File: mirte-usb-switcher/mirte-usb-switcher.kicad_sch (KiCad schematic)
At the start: 5 parts, among them J1 Conn_02x02_Counter_Clockwise, U1 SIP32509DT-T1-GE3

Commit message: move usb switcher
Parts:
- removed J1: Conn_02x02_Counter_Clockwise, Connector_PinHeader_2.54mm:PinHeader_2x02_P2.54mm_Vertical, symbol Connector_Generic:Conn_02x02_Counter_Clockwise
- removed USB1: U254-051T-4BH83-S1S, lcsc:MICRO-USB-SMD_U254-051T-4BH83-S1S, symbol lcsc:U254-051T-4BH83-S1S
- added C1: 100nF, Capacitor_SMD:C_0805_2012Metric, symbol Device:C
- added C2: 10uF, Capacitor_SMD:C_0805_2012Metric, symbol Device:C
- added D1, D2, D3, D4: LED, LED_SMD:LED_0805_2012Metric, symbol Device:LED
- added J1: Conn_02x04_Odd_Even, Connector_PinSocket_2.54mm:PinSocket_2x04_P2.54mm_Vertical, symbol Connector_Generic:Conn_02x04_Odd_Even
- added J2: Conn_01x04_Pin, Connector_PinHeader_2.54mm:PinHeader_1x04_P2.54mm_Vertical, symbol Connector:Conn_01x04_Pin
- added J3: USB_B_Micro, Connector_USB:USB_Micro-AB_Molex_47590-0001, symbol Connector:USB_B_Micro
- added R2, R3, R4, R5: R, Resistor_SMD:R_0805_2012Metric, symbol Device:R
- U1: footprint TSOT-23-6_L2.9-W1.6-P0.95-LS2.8-BL -> sip.pretty:TSOT-23-6_L2.9-W1.6-P0.95-LS2.8-BL
- USB2: footprint USB-A-TH_AF-WJDG -> usb.pretty:USB-A-TH_AF-WJDG
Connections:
- net D+: now also J3.3 (D+)
- net D-: now also J3.2 (D-)
- net GND: now also C1.2, C2.2, D1.1 (K), D2.1 (K), D3.1 (K), D4.1 (K), J1.5 (Pin_5), J3.5 (GND), J3.6 (Shield)
- net VOUT: now reaches U1.1 (OUT), U1.2 (OUT), USB2.1 (VCC)
- net VOUT: now also C1.1, C2.1
- net VIN: now reaches U1.5 (IN), U1.6 (IN)
- net VIN: now also J3.1 (VBUS)
- net SW renamed GPIO4_A4
- net GPIO4_A4: now also J1.8 (Pin_8), J2.4 (Pin_4), R4.1
- new net: D1.2 (A), R2.2
- new net: D2.2 (A), R3.2
- new net: D4.2 (A), R5.2
- new net: D3.2 (A), R4.2
- new net +3V3: J1.2 (Pin_2)
- new net +5V: J1.1 (Pin_1), J1.3 (Pin_3)
- new net GPIO0_D1: J1.7 (Pin_7), J2.3 (Pin_3), R5.1
- new net GPIO4_B4: J1.4 (Pin_4), J2.1 (Pin_1), R3.1
- new net GPIO4_B5: J1.6 (Pin_6), J2.2 (Pin_2), R2.1
- no-connect marks 2 -> 3

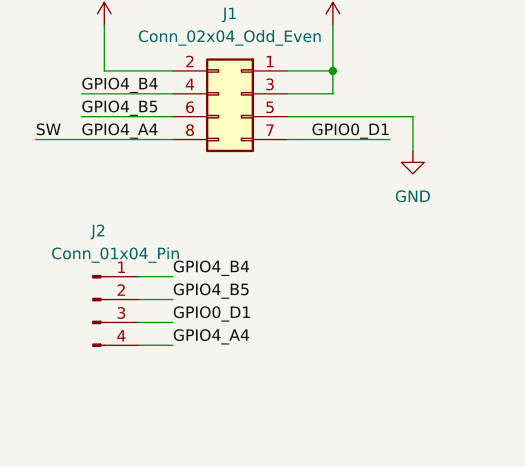
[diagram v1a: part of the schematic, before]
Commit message: usb switcher done
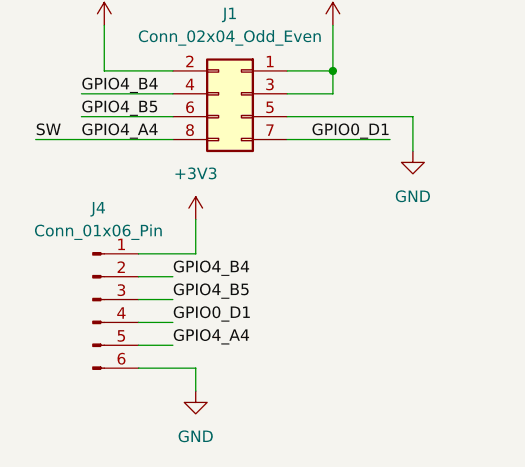
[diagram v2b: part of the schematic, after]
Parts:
- removed J2: Conn_01x04_Pin, Connector_PinHeader_2.54mm:PinHeader_1x04_P2.54mm_Vertical, symbol Connector:Conn_01x04_Pin
- added J4: Conn_01x06_Pin, Connector_PinHeader_2.54mm:PinHeader_1x06_P2.54mm_Vertical, symbol Connector:Conn_01x06_Pin
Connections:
- net +3V3: now also J4.1 (Pin_1)
- net GND: now also J4.6 (Pin_6)
- net GPIO0_D1: now also J4.4 (Pin_4)
- net GPIO4_A4: now also J4.5 (Pin_5)
- net GPIO4_B4: now also J4.2 (Pin_2)
- net GPIO4_B5: now also J4.3 (Pin_3)
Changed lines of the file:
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@@
+    (stroke (width 0) (type default))
+  )
+  (wire (pts (xy 66.04 118.11) (xy 66.04 115.57))
     (stroke (width 0) (type default))
   )
@@
     (stroke (width 0) (type default))
   )
+  (wire (pts (xy 66.04 115.57) (xy 59.69 115.57))
+    (stroke (width 0) (type default))
+  )
   (wire (pts (xy 156.21 39.37) (xy 172.72 39.37))
     (stroke (width 0) (type default))
@@
     (stroke (width 0) (type default))
   )
+  (wire (pts (xy 66.04 99.06) (xy 66.04 102.87))
+    (stroke (width 0) (type default))
+  )
   (wire (pts (xy 154.94 86.36) (xy 154.94 87.63))
     (stroke (width 0) (type default))
@@
   )
   (wire (pts (xy 154.94 95.25) (xy 154.94 99.06))
+    (stroke (width 0) (type default))
+  )
+  (wire (pts (xy 66.04 102.87) (xy 59.69 102.87))
     (stroke (width 0) (type default))
   )
@@
     )
   )
+  (symbol (lib_id "power:+3V3") (at 66.04 99.06 0) (unit 1)
+    (in_bom yes) (on_board yes) (dnp no) (fields_autoplaced)
+    (property "Reference" "#PWR014" (at 66.04 102.87 0)
+      (effects (font (size 1.27 1.27)) hide)
+    )
+    (property "Value" "+3V3" (at 66.04 93.98 0)
+      (effects (font (size 1.27 1.27)))
+    )
+    (property "Footprint" "" (at 66.04 99.06 0)
+      (effects (font (size 1.27 1.27)) hide)
+    )
+    (property "Datasheet" "" (at 66.04 99.06 0)
+      (effects (font (size 1.27 1.27)) hide)
+    )
+    (pin "1")
+    (instances
+      (project "mirte-usb-switcher"
+        (path "/8ab0622e-ffcf-4077-a1ef-4ead94df8977"
+          (reference "#PWR014") (unit 1)
+        )
+      )
+    )
+  )
   (symbol (lib_id "usb:AF90°WJDG") (at 182.88 41.91 0) (mirror y) (unit 1)
     (in_bom yes) (on_board yes) (dnp no) (fields_autoplaced)
@@
         (path "/8ab0622e-ffcf-4077-a1ef-4ead94df8977"
           (reference "#PWR09") (unit 1)
+        )
+      )
+    )
+  )
+  (symbol (lib_id "power:GND") (at 66.04 118.11 0) (unit 1)
+    (in_bom yes) (on_board yes) (dnp no) (fields_autoplaced)
+    (property "Reference" "#PWR015" (at 66.04 124.46 0)
+      (effects (font (size 1.27 1.27)) hide)
+    )
+    (property "Value" "GND" (at 66.04 123.19 0)
+      (effects (font (size 1.27 1.27)))
+    )
+    (property "Footprint" "" (at 66.04 118.11 0)
+      (effects (font (size 1.27 1.27)) hide)
+    )
+    (property "Datasheet" "" (at 66.04 118.11 0)
+      (effects (font (size 1.27 1.27)) hide)
+    )
+    (pin "1")
+    (instances
+      (project "mirte-usb-switcher"
+        (path "/8ab0622e-ffcf-4077-a1ef-4ead94df8977"
+          (reference "#PWR015") (unit 1)
         )
       )
@@
         (path "/8ab0622e-ffcf-4077-a1ef-4ead94df8977"
           (reference "C1") (unit 1)
+        )
+      )
+    )
+  )
+  (symbol (lib_id "Connector:Conn_01x06_Pin") (at 54.61 107.95 0) (unit 1)
+    (in_bom yes) (on_board yes) (dnp no) (fields_autoplaced)
+    (property "Reference" "J4" (at 55.245 97.79 0)
+      (effects (font (size 1.27 1.27)))
+    )
+    (property "Value" "Conn_01x06_Pin" (at 55.245 100.33 0)
+      (effects (font (size 1.27 1.27)))
+    )
+    (property "Footprint" "Connector_PinHeader_2.54mm:PinHeader_1x06_P2.54mm_Vertical" (at 54.61 107.95 0)
+      (effects (font (size 1.27 1.27)) hide)
+    )
+    (property "Datasheet" "~" (at 54.61 107.95 0)
+      (effects (font (size 1.27 1.27)) hide)
+    )
+    (pin "6")
+    (pin "1")
+    (pin "3")
+    (pin "4")
+    (pin "5")
+    (pin "2")
+    (instances
+      (project "mirte-usb-switcher"
+        (path "/8ab0622e-ffcf-4077-a1ef-4ead94df8977"
+          (reference "J4") (unit 1)
         )
       )
@@
         )
       )
-    )
-  )
-  (symbol (lib_id "Connector:Conn_01x04_Pin") (at 54.61 107.95 0) (unit 1)
-    (in_bom yes) (on_board yes) (dnp no)
-    (property "Reference" "J2" (at 55.245 100.33 0)
-      (effects (font (size 1.27 1.27)))
-    )
-    (property "Value" "Conn_01x04_Pin" (at 57.15 102.87 0)
-      (effects (font (size 1.27 1.27)))
-    )
-    (property "Footprint" "Connector_PinHeader_2.54mm:PinHeader_1x04_P2.54mm_Vertical" (at 54.61 107.95 0)
-      (effects (font (size 1.27 1.27)) hide)
-    )
-    (property "Datasheet" "~" (at 54.61 107.95 0)
-      (effects (font (size 1.27 1.27)) hide)
-    )
-    (pin "4")
-    (pin "3")
-    (pin "1")
-    (pin "2")
-    (instances
-      (project "mirte-usb-switcher"
-        (path "/8ab0622e-ffcf-4077-a1ef-4ead94df8977"
-          (reference "J2") (unit 1)
-        )
-      )

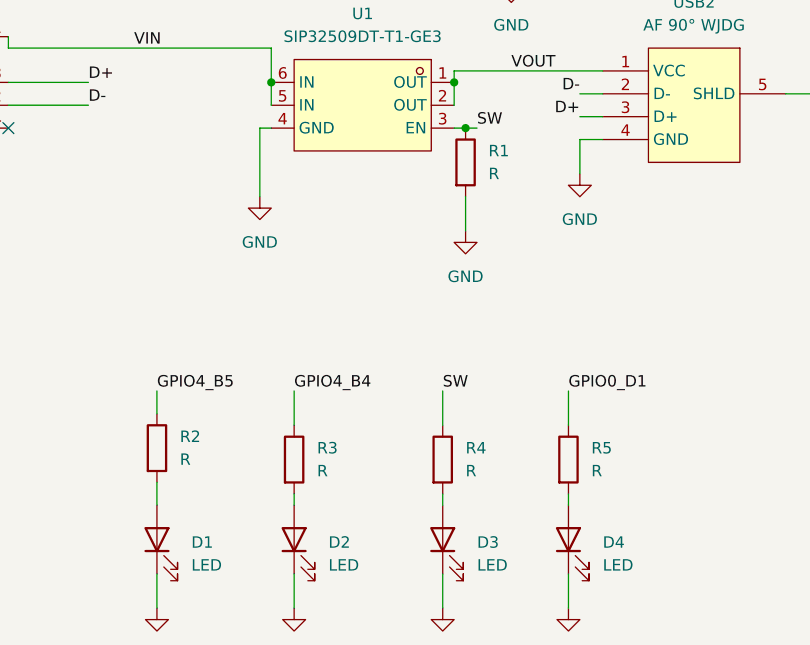
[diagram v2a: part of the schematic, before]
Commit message: Fixes lcsc shortage
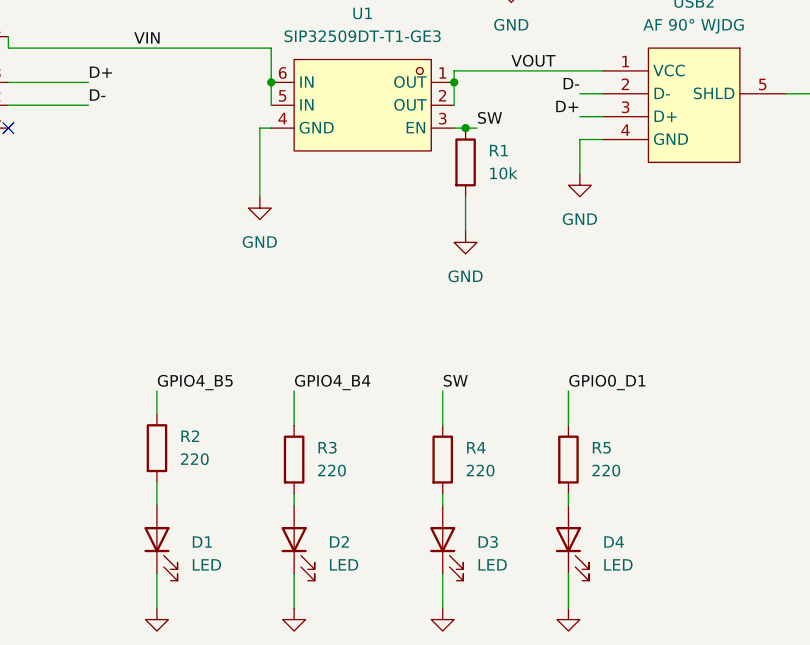
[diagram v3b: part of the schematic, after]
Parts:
- R1: value R -> 10k
- R2, R3, R4, R5: value R -> 220
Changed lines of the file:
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@@
       (effects (font (size 1.27 1.27)) (justify left))
     )
-    (property "Value" "R" (at 160.02 50.8 0)
+    (property "Value" "10k" (at 160.02 50.8 0)
       (effects (font (size 1.27 1.27)) (justify left))
     )
@@
       (effects (font (size 1.27 1.27)) (justify left))
     )
-    (property "Value" "R" (at 125.73 82.55 0)
+    (property "Value" "220" (at 125.73 82.55 0)
       (effects (font (size 1.27 1.27)) (justify left))
     )
@@
       (effects (font (size 1.27 1.27)) (justify left))
     )
-    (property "Value" "R" (at 140.97 83.82 0)
+    (property "Value" "220" (at 140.97 83.82 0)
       (effects (font (size 1.27 1.27)) (justify left))
     )
@@
       (effects (font (size 1.27 1.27)) (justify left))
     )
-    (property "Value" "R" (at 171.45 83.82 0)
+    (property "Value" "220" (at 171.45 83.82 0)
       (effects (font (size 1.27 1.27)) (justify left))
     )
@@
       (effects (font (size 1.27 1.27)) (justify left))
     )
-    (property "Value" "R" (at 157.48 83.82 0)
-      (effects (font (size 1.27 1.27)) (justify left))
-    )
+    (property "Value" "220" (at 157.48 83.82 0)
+      (effects (font (size 1.27 1.27)) (justify left))
+    )

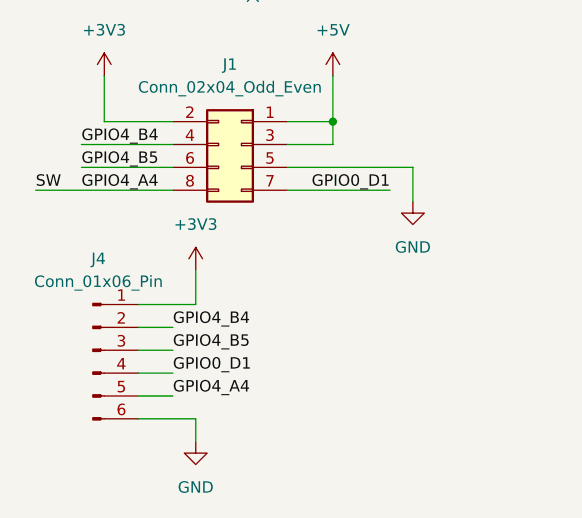
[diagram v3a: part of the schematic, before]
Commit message: Fix errors(wrong gpio, flipped 5v&gnd)
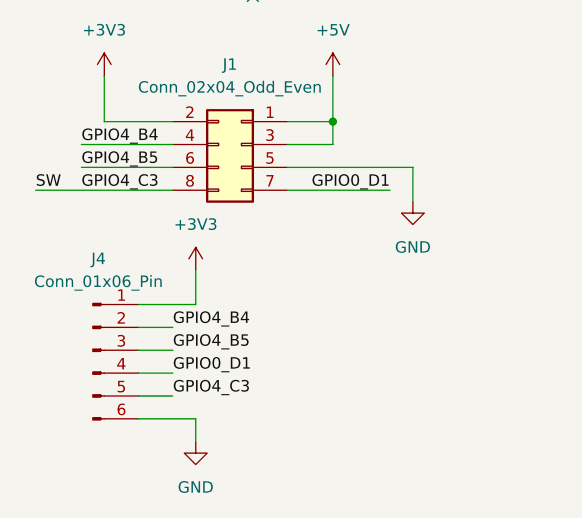
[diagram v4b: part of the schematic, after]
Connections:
- net GPIO4_A4 renamed GPIO4_C3
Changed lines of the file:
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@@
     (effects (font (size 1.27 1.27)) (justify left bottom))
   )
-  (label "GPIO4_A4" (at 53.34 90.17 0) (fields_autoplaced)
-    (effects (font (size 1.27 1.27)) (justify left bottom))
-  )
-  (label "GPIO4_A4" (at 63.5 113.03 0) (fields_autoplaced)
+  (label "GPIO4_C3" (at 53.34 90.17 0) (fields_autoplaced)
     (effects (font (size 1.27 1.27)) (justify left bottom))
   )
@@
     (effects (font (size 1.27 1.27)) (justify left bottom))
   )
+  (label "GPIO4_C3" (at 63.5 113.03 0) (fields_autoplaced)
+    (effects (font (size 1.27 1.27)) (justify left bottom))
+  )

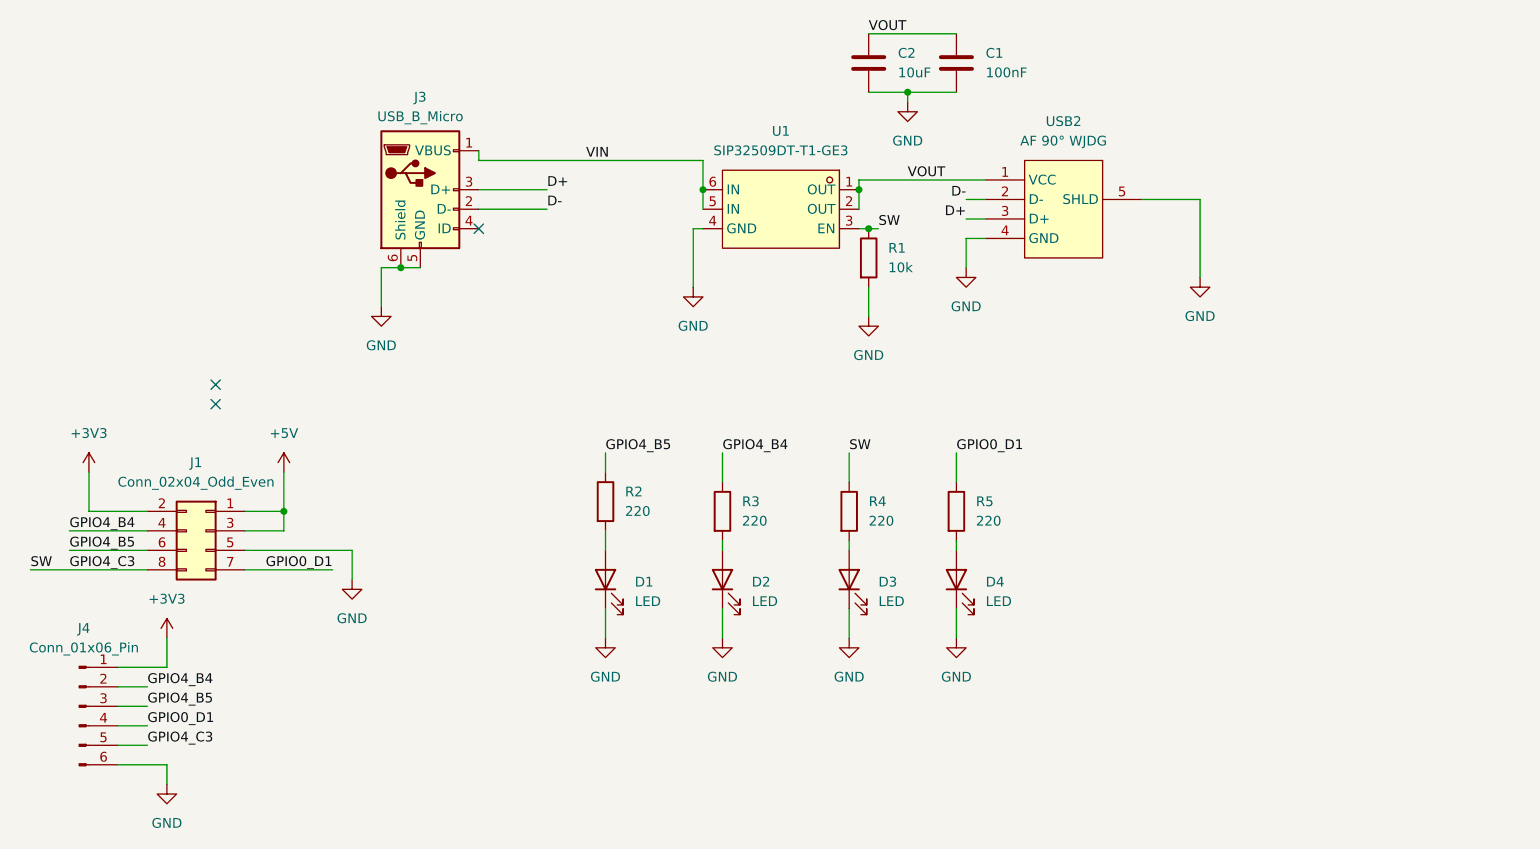
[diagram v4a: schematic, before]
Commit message: Add emergency switch by using mosfet for power
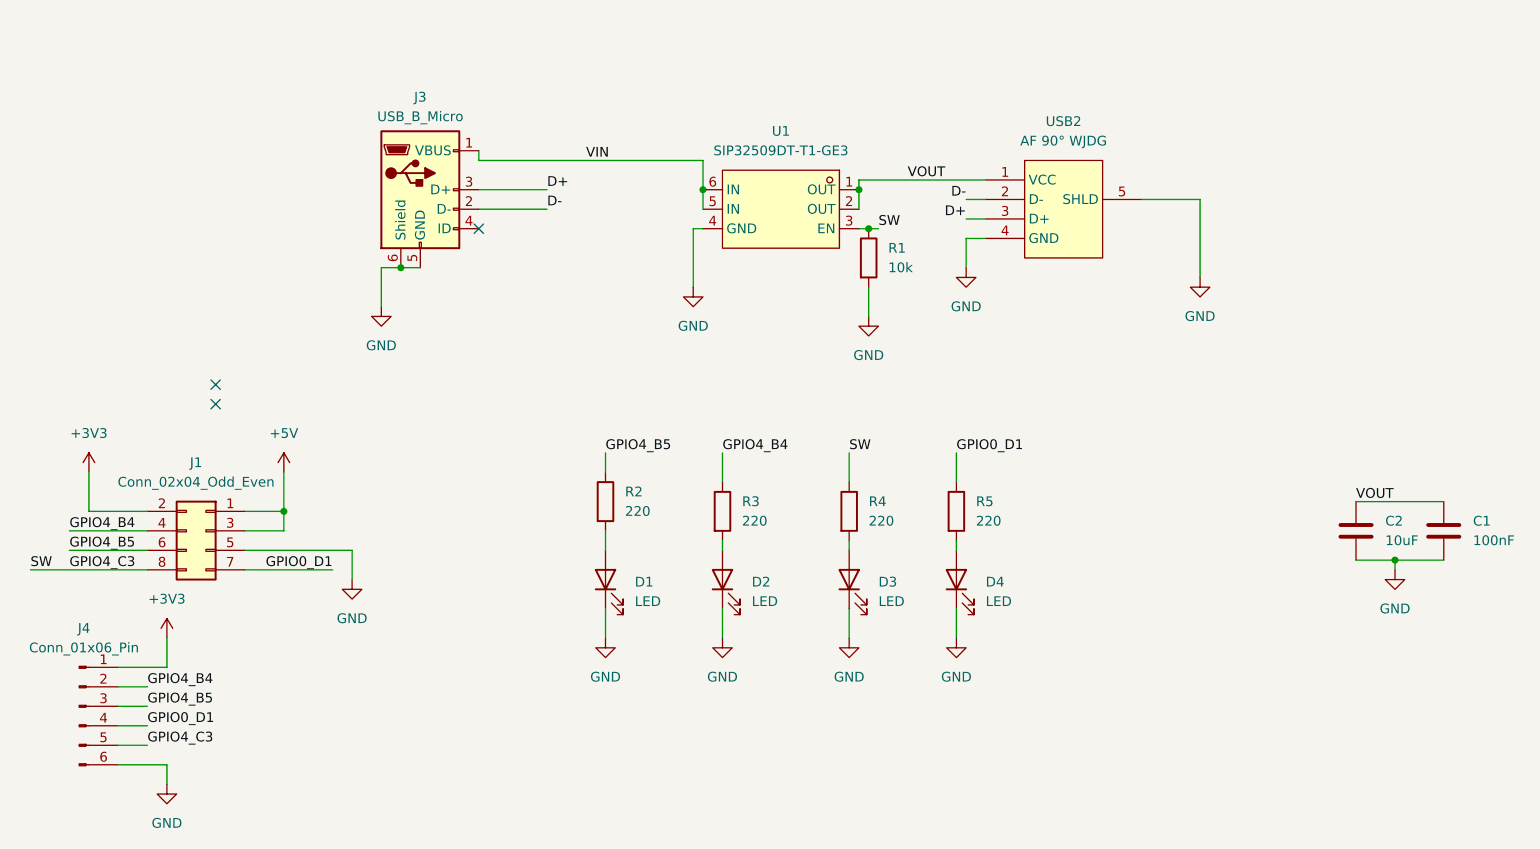
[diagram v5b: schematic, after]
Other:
- moved on the sheet: C1, C2

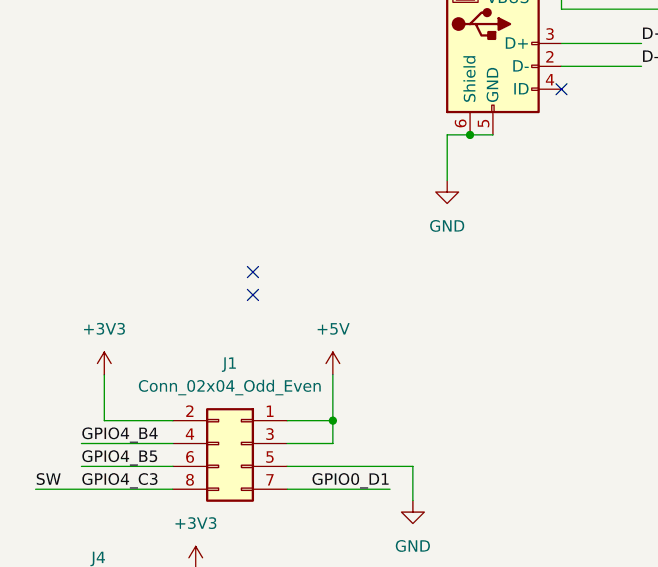
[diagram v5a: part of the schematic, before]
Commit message: Upd, add feetech servo connector
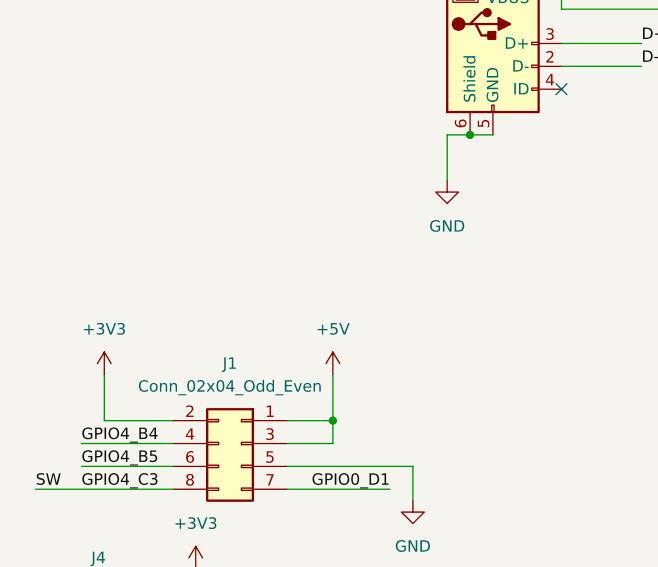
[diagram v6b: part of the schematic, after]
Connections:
- no-connect marks 3 -> 1
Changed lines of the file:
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@@
 		(at 106.68 45.72)
-	)
-	(no_connect
-		(at 72.39 66.04)
-	)
-	(no_connect
-		(at 72.39 68.58)
 	)
 	(wire
